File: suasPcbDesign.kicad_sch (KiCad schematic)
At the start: 80 parts, among them J1 SENSE_IB, J2 USB_C_Receptacle_USB2.0_16P, J3 5V Test Pad, J4 3V3 Test Pad, J5 ESC CTRL, J6 JTAG Pinout, SW1 SW_SPST, SW2 SW_SPST, U1 LMR51625DDC, U2 MCP3562RT-E/ST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

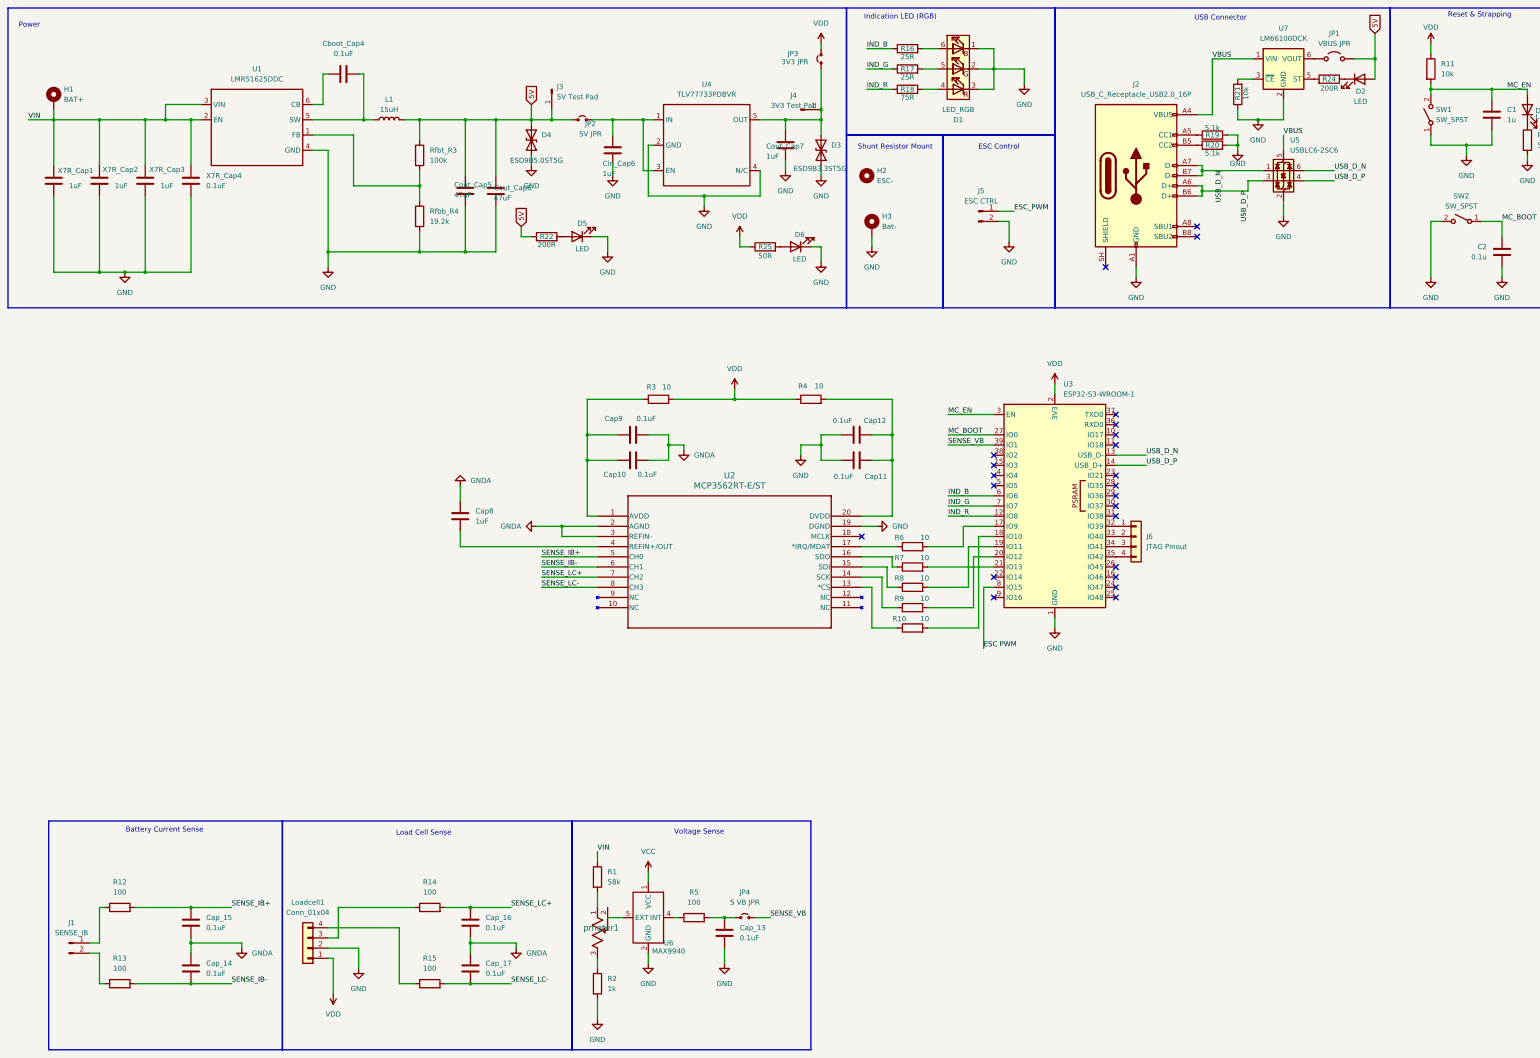
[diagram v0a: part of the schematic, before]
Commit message: Simplify voltage clamping circuit for voltage sensor
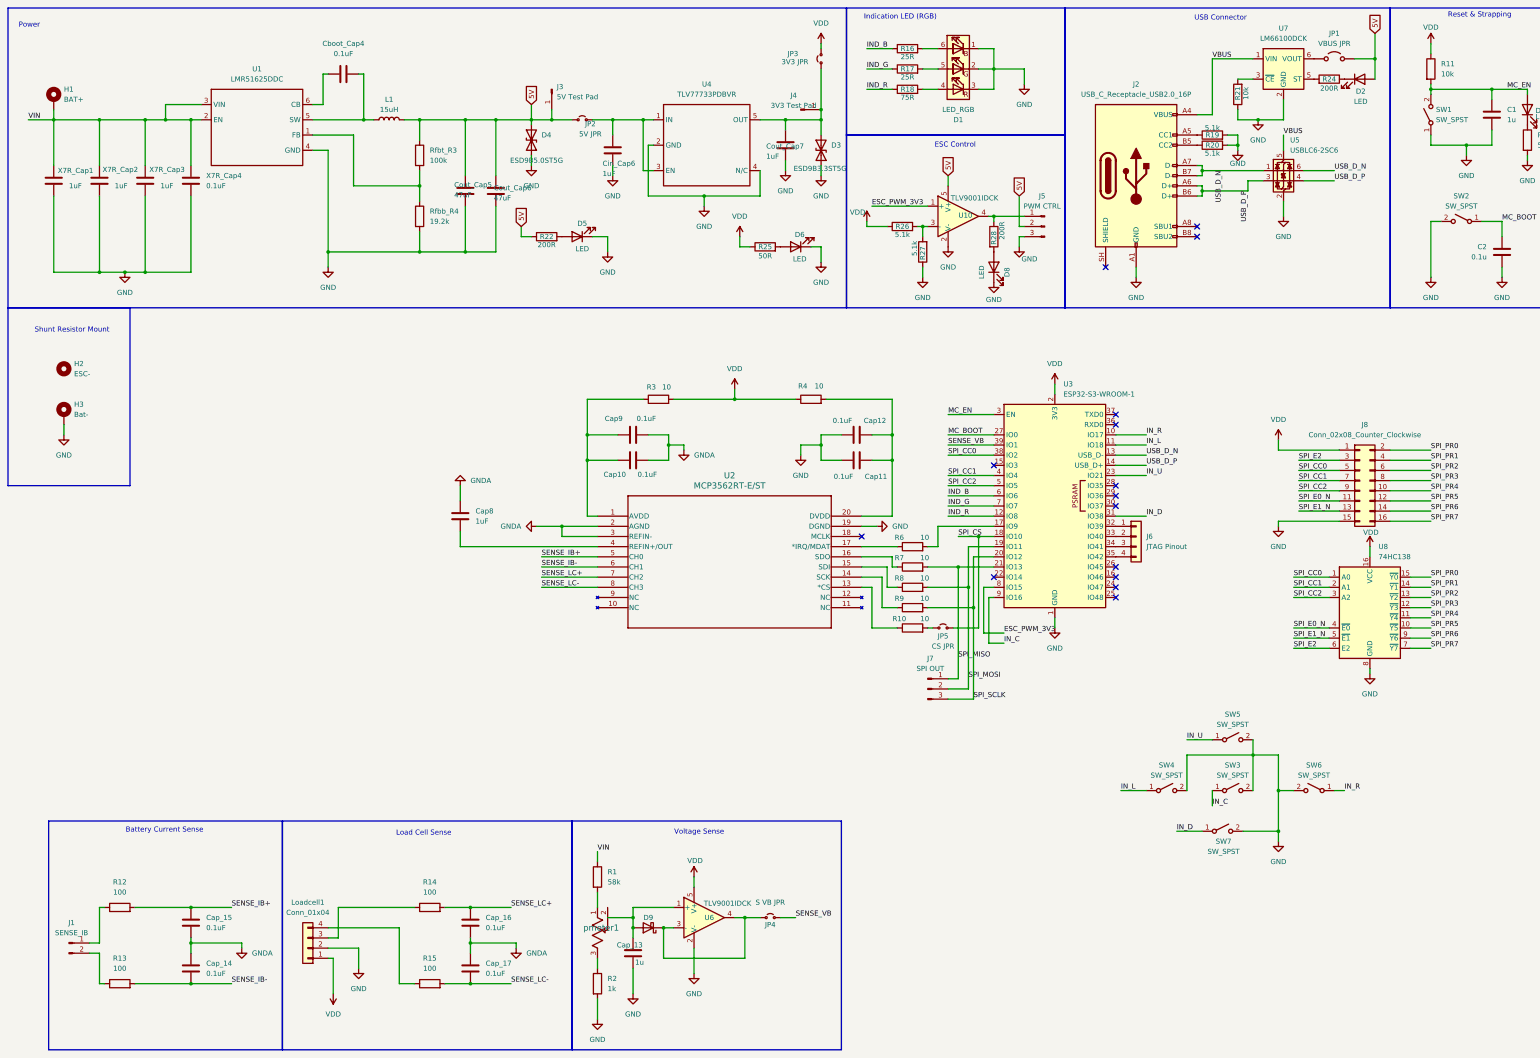
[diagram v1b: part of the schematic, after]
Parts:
- removed J5: ESC CTRL, Connector_Wire:SolderWire-1sqmm_1x02_P5.4mm_D1.4mm_OD2.7mm, symbol Connector:Conn_01x02_Pin
- removed R5: 100, Resistor_SMD:R_0603_1608Metric_Pad0.98x0.95mm_HandSolder, symbol Device:R
- removed U6: MAX9940, Package_TO_SOT_SMD:SOT-353_SC-70-5, symbol Custom:MAX9940
- added D8: LED, LED_SMD:LED_0603_1608Metric_Pad1.05x0.95mm_HandSolder, symbol Device:LED
- added D9: D_Schottky, Diode_SMD:D_0603_1608Metric_Pad1.05x0.95mm_HandSolder, symbol Device:D_Schottky
- added J5: PWM CTRL, Connector_PinSocket_2.54mm:PinSocket_1x03_P2.54mm_Vertical, symbol Connector:Conn_01x03_Pin
- added J7: SPI OUT, Connector_PinHeader_2.54mm:PinHeader_1x03_P2.54mm_Vertical, symbol Connector:Conn_01x03_Pin
- added J8: Conn_02x08_Counter_Clockwise, Connector_PinHeader_2.54mm:PinHeader_2x08_P2.54mm_Vertical, symbol Connector_Generic:Conn_02x08_Counter_Clockwise
- added JP5: CS JPR, symbol Jumper:Jumper_2_Small_Open
- added R26, R27: 5.1k, Resistor_SMD:R_0603_1608Metric_Pad0.98x0.95mm_HandSolder, symbol Device:R
- added R28: 200R, symbol Device:R
- added SW3, SW4, SW5, SW6, SW7: SW_SPST, Button_Switch_THT:SW_PUSH_1P1T_6x3.5mm_H4.3_APEM_MJTP1243, symbol Switch:SW_SPST
- added U10, U6: TLV9001IDCK, Package_TO_SOT_SMD:SOT-353_SC-70-5, symbol Amplifier_Operational:TLV9001IDCK
- added U8: 74HC138, Package_SO:TSSOP-16_4.4x5mm_P0.65mm, symbol 74xx:74HC138
- Cap_13: value 0.1uF -> 1u
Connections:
- net 5V: now also J5.2 (Pin_2), U10.5 (V+)
- net GND: now also D8.1 (K), J5.3 (Pin_3), J8.15 (Pin_15), R27.1, SW3.2 (B), SW4.2 (B), SW5.2 (B), SW6.2 (B), SW7.2 (B), U10.2 (V-), U6.2 (V-), U8.8 (GND)
- net VDD: now also J8.1 (Pin_1), R26.1, U6.5 (V+), U8.16 (VCC)
- net at Cap_13.1: now also pmeter1.2, D9.2 (A), U6.1 (+); no longer JP4.1 (A)
- net SPI_SCLK: now reaches R9.2, U3.20 (IO12)
- net SPI_SCLK: now also J7.3 (Pin_3)
- net SPI_MOSI: now reaches R8.2, U3.19 (IO11)
- net SPI_MOSI: now also J7.2 (Pin_2)
- net IN_R: now reaches U3.10 (IO17)
- net IN_R: now also SW6.1 (A)
- net IN_L: now reaches U3.11 (IO18)
- net IN_L: now also SW4.1 (A)
- net at R10.2: now also JP5.1 (A); no longer U3.18 (IO10)
- net SPI_MISO: now reaches R7.2, U3.21 (IO13)
- net SPI_MISO: now also J7.1 (Pin_1)
- net IN_U: now reaches U3.23 (IO21)
- net IN_U: now also SW5.1 (A)
- net IN_D: now reaches U3.31 (IO38)
- net IN_D: now also SW7.1 (A)
- net SPI_CC0: now reaches U3.38 (IO2)
- net SPI_CC0: now also J8.5 (Pin_5), U8.1 (A0)
- net SPI_CC1: now reaches U3.4 (IO4)
- net SPI_CC1: now also J8.7 (Pin_7), U8.2 (A1)
- net SPI_CC2: now reaches U3.5 (IO5)
- net SPI_CC2: now also J8.9 (Pin_9), U8.3 (A2)
- net IN_C: now reaches U3.9 (IO16)
- net IN_C: now also SW3.1 (A)
- net ESC PWM renamed ESC_PWM_3V3
- net ESC_PWM_3V3: now also U10.1 (+)
- new net: J5.1 (Pin_1), R28.1, U10.4
- new net: D8.2 (A), R28.2
- new net: D9.1 (K), JP4.1 (A), U6.3 (-), U6.4
- new net: R26.2, R27.2, U10.3 (-)
- new net SPI_CS: JP5.2 (B), U3.18 (IO10)
- new net SPI_E0_N: J8.11 (Pin_11), U8.4 (~{E0})
- new net SPI_E1_N: J8.13 (Pin_13), U8.5 (~{E1})
- new net SPI_E2: J8.3 (Pin_3), U8.6 (E2)
- new net SPI_PR0: J8.2 (Pin_2), U8.15 (~{Y0})
- new net SPI_PR1: J8.4 (Pin_4), U8.14 (~{Y1})
- new net SPI_PR2: J8.6 (Pin_6), U8.13 (~{Y2})
- new net SPI_PR3: J8.8 (Pin_8), U8.12 (~{Y3})
- new net SPI_PR4: J8.10 (Pin_10), U8.11 (~{Y4})
- new net SPI_PR5: J8.12 (Pin_12), U8.10 (~{Y5})
- new net SPI_PR6: J8.14 (Pin_14), U8.9 (~{Y6})
- new net SPI_PR7: J8.16 (Pin_16), U8.7 (~{Y7})
- no-connect marks 23 -> 15
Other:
- moved on the sheet: Cap_13, H2, H3, JP4

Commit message: Organize schematic
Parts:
- removed D9: D_Schottky, Diode_SMD:D_0603_1608Metric_Pad1.05x0.95mm_HandSolder, symbol Device:D_Schottky
- removed U10, U6: TLV9001IDCK, Package_TO_SOT_SMD:SOT-353_SC-70-5, symbol Amplifier_Operational:TLV9001IDCK
- added D9: CUS520_H3F, Custom:USC_TOS, symbol Custom:CUS520_H3F
- added U6: (no value), Package_TO_SOT_SMD:SOT-23-5_HandSoldering, symbol Custom:MCP6486RT-E/OT
- added U9: LMV331, Package_TO_SOT_SMD:SOT-23-5_HandSoldering, symbol Comparator:LMV331
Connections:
- net 5V: now also U9.5 (V+)
- net ESC_PWM_3V3: now also U9.1 (+)
- net GND: now also U6.5 (V-), U9.2 (V-)
- net SPI_CS: no longer JP5.2 (B)
- net SPI_MISO: now also J7.2 (Pin_2); no longer J7.1 (Pin_1)
- net SPI_MOSI: now also J7.1 (Pin_1); no longer J7.2 (Pin_2)
- net VDD: now also U6.2 (V+)
- net at J5.1 (Pin_1), R28.1: now also U9.4
- net at Cap_13.1, pmeter1.2: now also D9.2, U6.3 (+)
- net at JP4.1 (A): now also D9.1, U6.1, U6.4 (-)
- net ADC_IRQ: now reaches R6.2, U3.17 (IO9)
- net at R26.2, R27.2: now also U9.3 (-)
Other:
- note added: "ADC"
- note added: "Input Btns"
- note added: "SPI Breakout"
- moved on the sheet: Cap10, Cap11, Cap12, Cap8, Cap9, Cap_13, Cap_14, Cap_15, Cap_16, Cap_17, H2, H3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

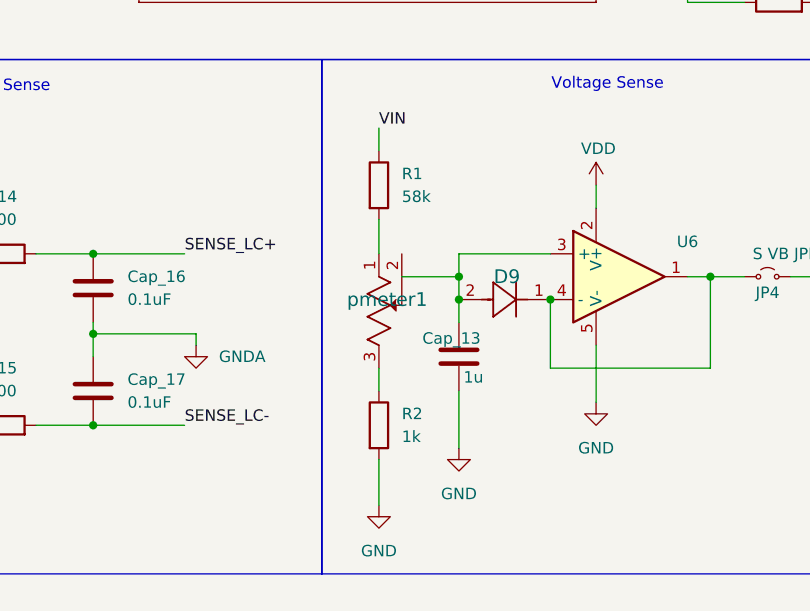
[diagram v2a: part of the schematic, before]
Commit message: Replace trim pot
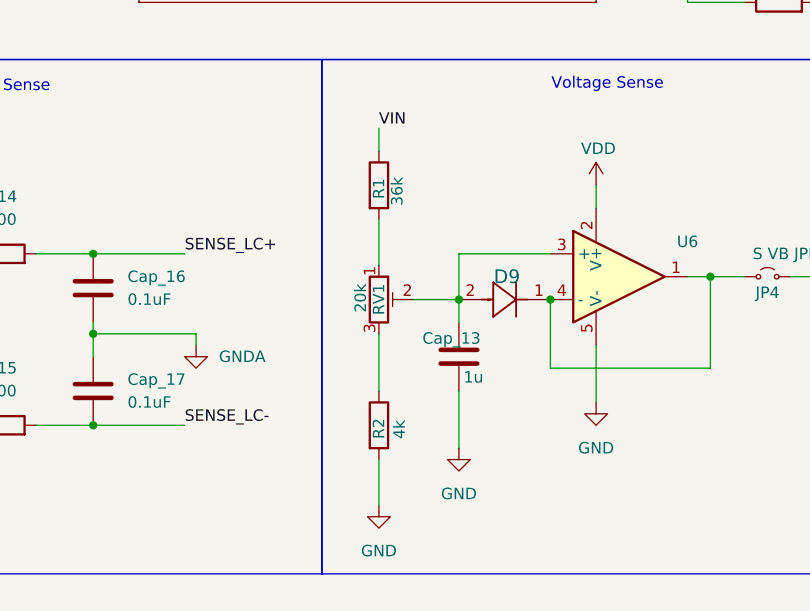
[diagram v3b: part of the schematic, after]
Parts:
- removed pmeter1: 23BR1KLFTR, RES3_23B_TTE, symbol suasPcbSymbols:23BR1KLFTR
- added RV1: 20k, Potentiometer_THT:Potentiometer_Bourns_3386P_Vertical, symbol Device:R_Potentiometer_Trim
- R1: value 58k -> 36k
- R2: value 1k -> 4k
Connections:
- net at R1.2: now also RV1.1
- net at Cap_13.1, D9.2, U6.3 (+): now also RV1.2
- net at R2.1: now also RV1.3
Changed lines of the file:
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@@
 	)
 	(junction
-		(at 162.56 190.5)
-		(diameter 0)
-		(color 0 0 0 0)
-	)
-	(junction
 		(at 147.32 44.45)
 		(diameter 0)
@@
 	(wire
 		(pts
-			(xy 156.21 190.5) (xy 162.56 190.5)
-		)
-		(stroke
-			(width 0)
-			(type default)
-		)
-	)
-	(wire
-		(pts
 			(xy 54.61 151.13) (xy 59.69 151.13)
 		)
@@
 	(wire
 		(pts
-			(xy 162.56 187.96) (xy 162.56 190.5)
-		)
-		(stroke
-			(width 0)
-			(type default)
-		)
-	)
-	(wire
-		(pts
 			(xy 292.1 209.55) (xy 299.72 209.55)
 		)
@@
 	(wire
 		(pts
-			(xy 153.67 200.66) (xy 153.67 203.2)
+			(xy 153.67 196.85) (xy 153.67 203.2)
 		)
 		(stroke
@@
 	(wire
 		(pts
+			(xy 157.48 193.04) (xy 162.56 193.04)
+		)
+		(stroke
+			(width 0)
+			(type default)
+		)
+	)
+	(wire
+		(pts
 			(xy 245.11 81.28) (xy 245.11 83.82)
 		)
@@
 	(wire
 		(pts
-			(xy 162.56 190.5) (xy 162.56 193.04)
+			(xy 162.56 187.96) (xy 162.56 193.04)
 		)
 		(stroke
@@
 	(wire
 		(pts
-			(xy 153.67 184.15) (xy 153.67 187.96)
+			(xy 153.67 184.15) (xy 153.67 189.23)
 		)
 		(stroke
@@
 		(dnp no)
 		(property "Reference" "R1"
-			(at 156.21 179.0699 0)
+			(at 153.67 181.864 90)
 			(show_name no)
 			(do_not_autoplace no)
@@
 			)
 		)
-		(property "Value" "58k"
-			(at 156.21 181.6099 0)
+		(property "Value" "36k"
+			(at 155.702 182.626 90)
 			(show_name no)
 			(do_not_autoplace no)
@@
 	)
 	(symbol
-		(lib_id "suasPcbSymbols:23BR1KLFTR")
-		(at 153.67 187.96 270)
-		(unit 1)
-		(body_style 1)
-		(exclude_from_sim no)
-		(in_bom yes)
-		(on_board yes)
-		(in_pos_files yes)
-		(dnp no)
-		(property "Reference" "pmeter1"
-			(at 150.114 193.04 90)
-			(show_name no)
-			(do_not_autoplace no)
-			(effects
-				(font
-					(size 1.524 1.524)
-				)
-				(justify left)
-			)
-		)
-		(property "Value" "23BR1KLFTR"
-			(at 148.336 195.326 90)
-			(hide yes)
-			(show_name no)
-			(do_not_autoplace no)
-			(effects
-				(font
-					(size 1.524 1.524)
-				)
-				(justify left)
-			)
-		)
-		(property "Footprint" "RES3_23B_TTE"
-			(at 153.67 187.96 0)
-			(hide yes)
-			(show_name no)
-			(do_not_autoplace no)
-			(effects
-				(font
-					(size 1.27 1.27)
-					(italic yes)
-				)
-			)
-		)
-		(property "Datasheet" "23BR1KLFTR"
-			(at 153.67 187.96 0)
-			(hide yes)
-			(show_name no)
-			(do_not_autoplace no)
-			(effects
-				(font
-					(size 1.27 1.27)
-					(italic yes)
-				)
-			)
-		)
-		(property "Description" ""
-			(at 153.67 187.96 0)
-			(hide yes)
-			(show_name no)
-			(do_not_autoplace no)
-			(effects
-				(font
-					(size 1.27 1.27)
-				)
-			)
-		)
-		(pin "2"
-		)
-		(pin "3"
-		)
-		(pin "1"
-		)
-		(instances
-			(project "suasPcbDesign"
-				(path "/3f4829a2-0fac-45c0-b8b3-bdb72c54e399"
-					(reference "pmeter1")
-					(unit 1)
-				)
-			)
-		)
-	)
-	(symbol
 		(lib_id "Device:LED")
 		(at 158.75 73.66 180)
@@
 	)
 	(symbol
+		(lib_id "Device:R_Potentiometer_Trim")
+		(at 153.67 193.04 0)
+		(unit 1)
+		(body_style 1)
+		(exclude_from_sim no)
+		(in_bom yes)
+		(on_board yes)
+		(in_pos_files yes)
+		(dnp no)
+		(property "Reference" "RV1"
+			(at 153.67 191.262 90)
+			(show_name no)
+			(do_not_autoplace no)
+			(effects
+				(font
+					(size 1.27 1.27)
+				)
+				(justify right)
+			)
+		)
+		(property "Value" "20k"
+			(at 151.638 191.262 90)
+			(show_name no)
+			(do_not_autoplace no)
+			(effects
+				(font
+					(size 1.27 1.27)
+				)
+				(justify right)
+			)
+		)
+		(property "Footprint" "Potentiometer_THT:Potentiometer_Bourns_3386P_Vertical"
+			(at 153.67 193.04 0)
+			(hide yes)
+			(show_name no)
+			(do_not_autoplace no)
+			(effects
+				(font
+					(size 1.27 1.27)
+				)
+			)
+		)
+		(property "Datasheet" ""
+			(at 153.67 193.04 0)
+			(hide yes)
+			(show_name no)
+			(do_not_autoplace no)
+			(effects
+				(font
+					(size 1.27 1.27)
+				)
+			)
+		)
+		(property "Description" "Trim-potentiometer"
+			(at 153.67 193.04 0)
+			(hide yes)
+			(show_name no)
+			(do_not_autoplace no)
+			(effects
+				(font
+					(size 1.27 1.27)
+				)
+			)
+		)
+		(property "Sim.Device" "R"
+			(at 153.67 193.04 0)
+			(hide yes)
+			(show_name no)
+			(do_not_autoplace no)
+			(effects
+				(font
+					(size 1.27 1.27)
+				)
+			)
+		)
+		(property "Sim.Type" "POT"
+			(at 153.67 193.04 0)
+			(hide yes)
+			(show_name no)
+			(do_not_autoplace no)
+			(effects
+				(font
+					(size 1.27 1.27)
+				)
+			)
+		)
+		(property "Sim.Pins" "1=r0 2=wiper 3=r1"
+			(at 153.67 193.04 0)
+			(hide yes)
+			(show_name no)
+			(do_not_autoplace no)
+			(effects
+				(font
+					(size 1.27 1.27)
+				)
+			)
+		)
+		(pin "1"
+		)
+		(pin "2"
+		)
+		(pin "3"
+		)
+		(instances
+			(project "suasPcbDesign"
+				(path "/3f4829a2-0fac-45c0-b8b3-bdb72c54e399"
+					(reference "RV1")
+					(unit 1)
+				)
+			)
+		)
+	)
+	(symbol
 		(lib_id "power:GND")
 		(at 189.23 134.62 90)
@@
 		(in_pos_files yes)
 		(dnp no)
-		(fields_autoplaced yes)
 		(property "Reference" "R2"
-			(at 156.21 205.7399 0)
+			(at 153.67 208.534 90)
 			(show_name no)
 			(do_not_autoplace no)
@@
 			)
 		)
-		(property "Value" "1k"
-			(at 156.21 208.2799 0)
+		(property "Value" "4k"
+			(at 155.956 208.534 90)
 			(show_name no)
 			(do_not_autoplace no)

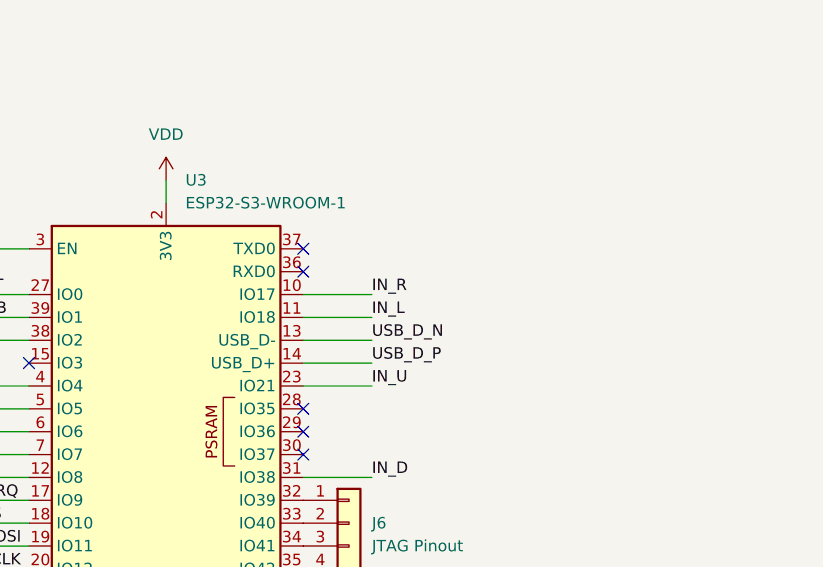
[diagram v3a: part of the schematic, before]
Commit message: Add decoupling caps to esp32 s3
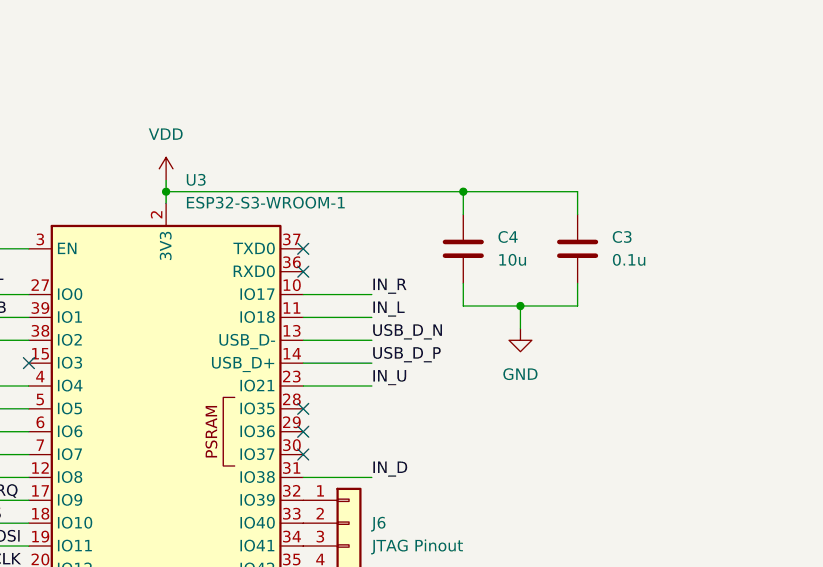
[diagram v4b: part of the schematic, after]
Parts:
- added C3: 0.1u, Capacitor_SMD:C_0603_1608Metric_Pad1.08x0.95mm_HandSolder, symbol Device:C
- added C4: 10u, Capacitor_SMD:C_0603_1608Metric_Pad1.08x0.95mm_HandSolder, symbol Device:C
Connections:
- net GND: now also C3.2, C4.2
- net VDD: now also C3.1, C4.1
